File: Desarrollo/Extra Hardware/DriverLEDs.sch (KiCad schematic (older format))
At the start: 36 parts, among them J1 VCC, Q1 BC548, Q2 BC548, Q3 BC548

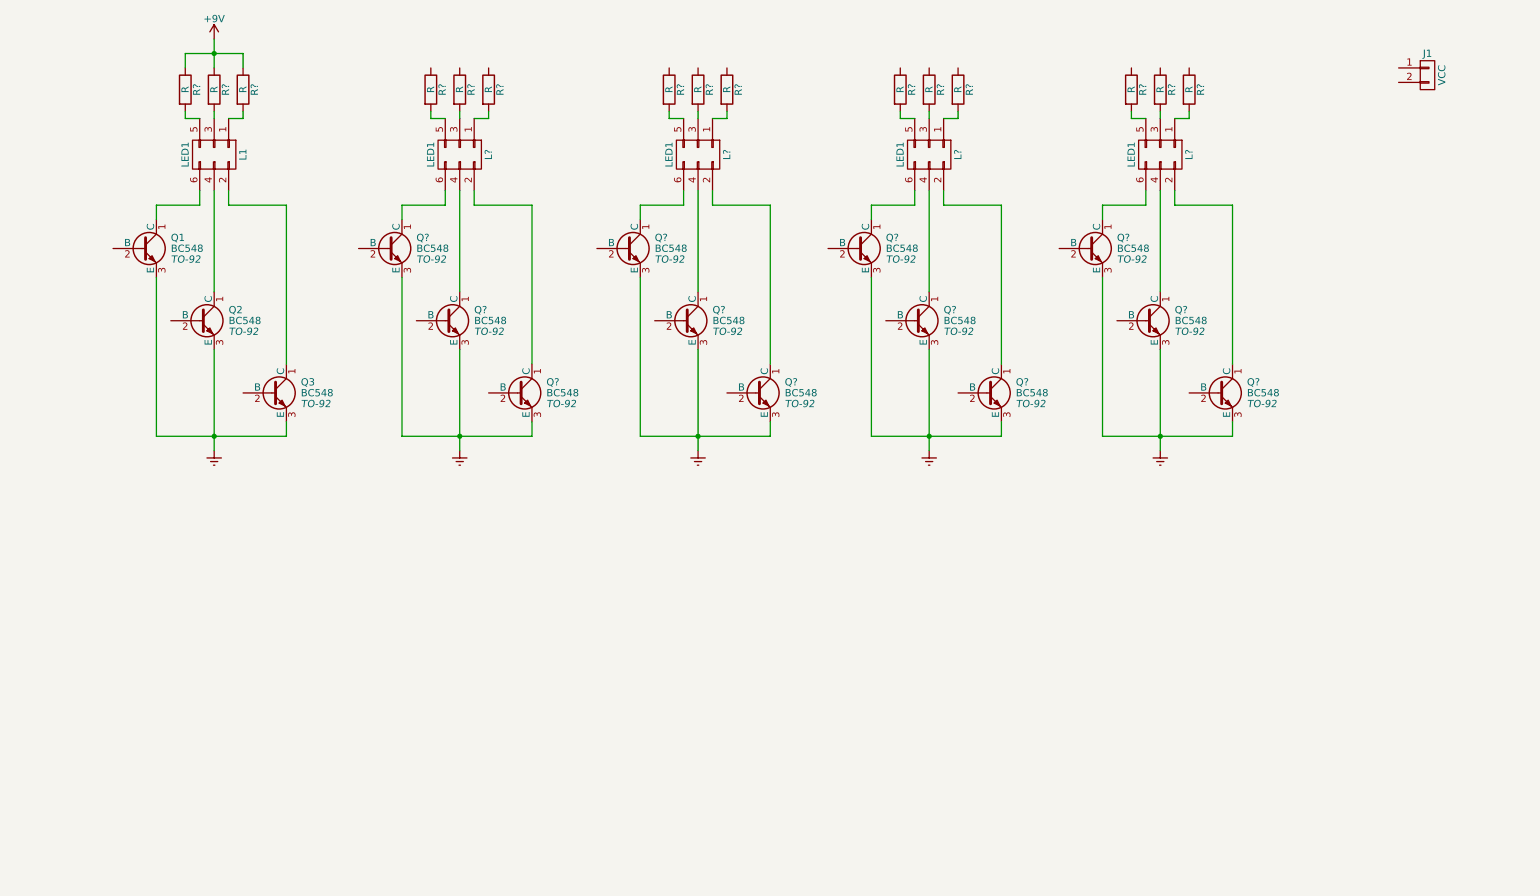
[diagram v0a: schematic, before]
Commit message: Actualización de esquemático, se completaron campos de "Hoja de dato" y "Código Digikey" para cada componente. Se completaron los rótulos de hojas. Versión Final de PCB. Actualización de tamaño de pistas y redimensión de zonas de relleno. Lista de Materiales actualizada en carpeta "Documentación".
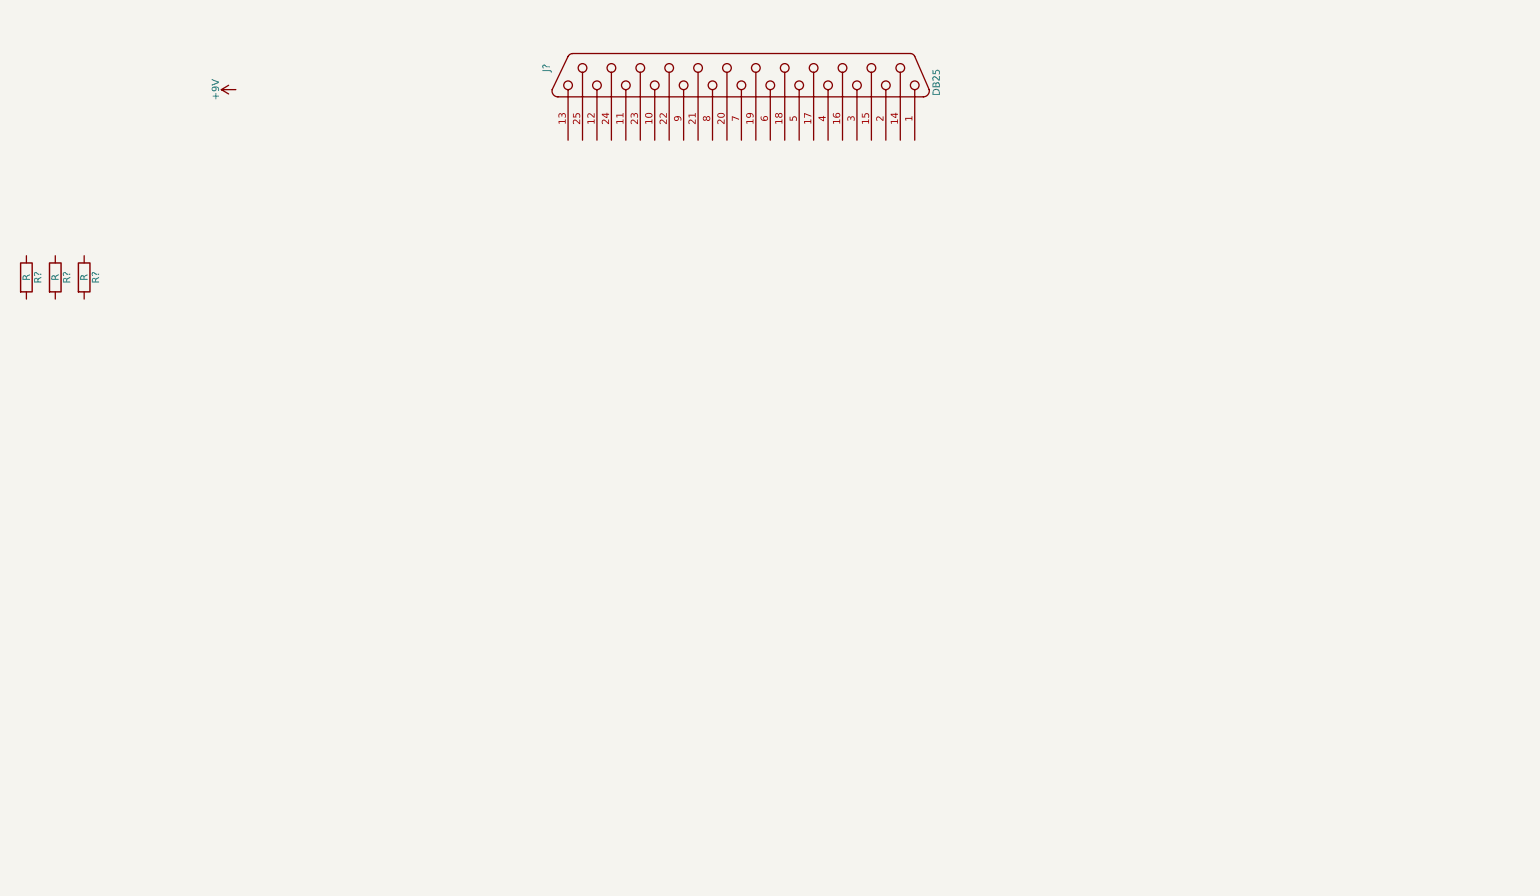
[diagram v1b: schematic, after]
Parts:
- removed J1: VCC, symbol CONN_01X02
- removed L1, L? (x4): LED1, symbol CONN_02X03
- removed Q1, Q2, Q3, Q? (x12): BC548, TO-92, symbol BC548
- removed R? (x15): R, symbol R
- added J?: DB25, symbol DB25
- added R? (x3): R, symbol R

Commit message: Desarrollo de placa de driver para manejo de leds de estimulación visual. Creación de esquemático y PCB correspondiente.
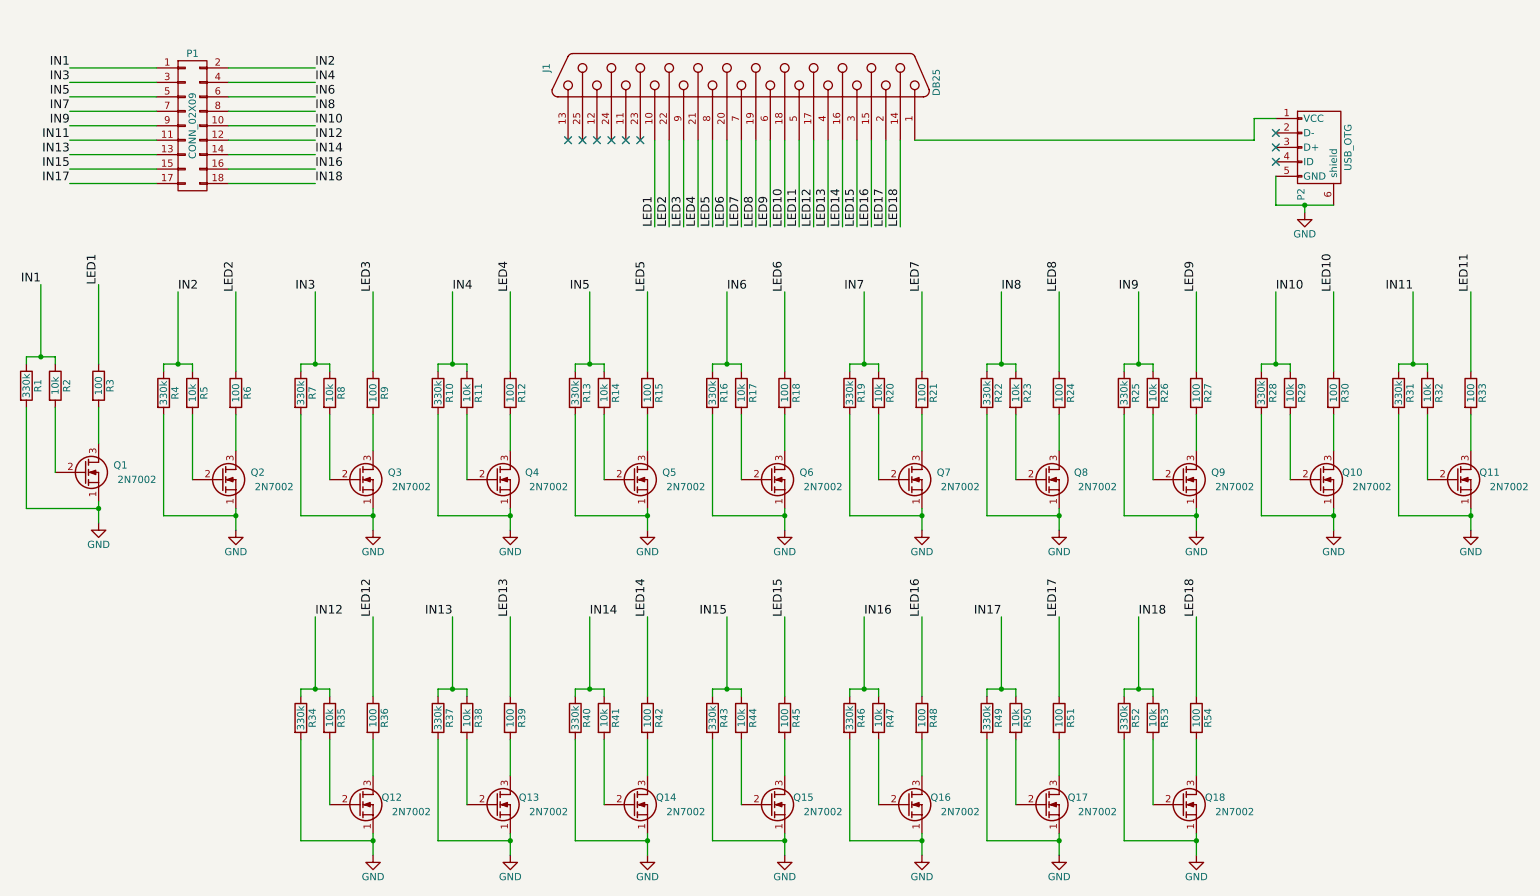
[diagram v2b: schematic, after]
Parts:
- added P1: CONN_02X09, Pin_Headers:Pin_Header_Straight_2x09, symbol CONN_02X09
- added P2: USB_OTG, Connect:USB_Micro-B, symbol USB_OTG
- added Q1, Q10, Q11, Q12, Q13, Q14, Q15, Q16, Q17, Q18, Q2, Q3, Q4, Q5, Q6, Q7, Q8, Q9: 2N7002, TO_SOT_Packages_SMD:SOT-23, symbol Q_NMOS_SGD
- added R10, R13, R16, R19, R22, R25, R28, R31, R34, R37, R4, R40, R43, R46, R49, R52, R7: 330k, DriverLeds:R_0805, symbol R
- added R11, R14, R17, R20, R23, R26, R29, R32, R35, R38, R41, R44, R47, R5, R50, R53, R8: 10k, DriverLeds:R_0805, symbol R
- added R12, R15, R18, R21, R24, R27, R30, R33, R36, R39, R42, R45, R48, R51, R54, R6, R9: 100, DriverLeds:R_0805, symbol R
- J1: renamed from J?; footprint (none) -> Connect:DB25FC
- R1: renamed from R?; value R -> 330k; footprint (none) -> DriverLeds:R_0805
- R2: renamed from R?; value R -> 10k; footprint (none) -> DriverLeds:R_0805
- R3: renamed from R?; value R -> 100; footprint (none) -> DriverLeds:R_0805
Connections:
- net at J1.1: now also P2.1 (VCC)
- net LED1: now reaches J1.10
- net LED1: now also R3.1
- net LED18: now reaches J1.14 (P14)
- net LED18: now also R54.1
- net LED16: now reaches J1.15 (P15)
- net LED16: now also R48.1
- net LED14: now reaches J1.16 (P16)
- net LED14: now also R42.1
- net LED12: now reaches J1.17 (P17)
- net LED12: now also R36.1
- net LED10: now reaches J1.18 (P18)
- net LED10: now also R30.1
- net LED8: now reaches J1.19 (P19)
- net LED8: now also R24.1
- net LED17: now reaches J1.2
- net LED17: now also R51.1
- net LED6: now reaches J1.20 (P20)
- net LED6: now also R18.1
- net LED4: now reaches J1.21 (P21)
- net LED4: now also R12.1
- net LED2: now reaches J1.22 (P22)
- net LED2: now also R6.1
- net LED15: now reaches J1.3
- net LED15: now also R45.1
- net LED13: now reaches J1.4
- net LED13: now also R39.1
- net LED11: now reaches J1.5
- net LED11: now also R33.1
- net LED9: now reaches J1.6
- net LED9: now also R27.1
- net LED7: now reaches J1.7
- net LED7: now also R21.1
- net LED5: now reaches J1.8
- net LED5: now also R15.1
- net LED3: now reaches J1.9
- net LED3: now also R9.1
- net IN1: now reaches R1.1
- net IN1: now also R2.1, P1.1 (P1)
- net GND: now reaches R1.2
- net GND: now also P2.5 (GND), P2.6 (shield), Q1.1 (S), Q10.1 (S), Q11.1 (S), Q12.1 (S), Q13.1 (S), Q14.1 (S), Q15.1 (S), Q16.1 (S), Q17.1 (S), Q18.1 (S), Q2.1 (S), Q3.1 (S), Q4.1 (S), Q5.1 (S), Q6.1 (S), Q7.1 (S), Q8.1 (S), Q9.1 (S), R10.2, R13.2, R16.2, R19.2, R22.2, R25.2, R28.2, R31.2, R34.2, R37.2, R4.2, R40.2, R43.2, R46.2, R49.2, R52.2, R7.2
- net at R2.2: now also Q1.2 (G)
- net at R3.2: now also Q1.3 (D)
- new net: Q2.2 (G), R5.2
- new net: Q2.3 (D), R6.2
- new net: Q3.2 (G), R8.2
- new net: Q3.3 (D), R9.2
- new net: Q4.2 (G), R11.2
- new net: Q4.3 (D), R12.2
- new net: Q5.2 (G), R14.2
- new net: Q5.3 (D), R15.2
- new net: Q6.2 (G), R17.2
- new net: Q6.3 (D), R18.2
- new net: Q7.2 (G), R20.2
- new net: Q7.3 (D), R21.2
- new net: Q8.2 (G), R23.2
- new net: Q8.3 (D), R24.2
- new net: Q9.2 (G), R26.2
- new net: Q9.3 (D), R27.2
- new net: Q10.2 (G), R29.2
- new net: Q10.3 (D), R30.2
- new net: Q11.2 (G), R32.2
- new net: Q11.3 (D), R33.2
- new net: Q12.2 (G), R35.2
- new net: Q12.3 (D), R36.2
- new net: Q13.2 (G), R38.2
- new net: Q13.3 (D), R39.2
- new net: Q14.2 (G), R41.2
- new net: Q14.3 (D), R42.2
- new net: Q15.2 (G), R44.2
- new net: Q15.3 (D), R45.2
- new net: Q16.2 (G), R47.2
- new net: Q16.3 (D), R48.2
- new net: Q17.2 (G), R50.2
- new net: Q17.3 (D), R51.2
- new net: Q18.2 (G), R53.2
- new net: Q18.3 (D), R54.2
- new net IN10: P1.10 (P10), R28.1, R29.1
- new net IN11: P1.11 (P11), R31.1, R32.1
- new net IN12: P1.12 (P12), R34.1, R35.1
- new net IN13: P1.13 (P13), R37.1, R38.1
- new net IN14: P1.14 (P14), R40.1, R41.1
- new net IN15: P1.15 (P15), R43.1, R44.1
- new net IN16: P1.16 (P16), R46.1, R47.1
- new net IN17: P1.17 (P17), R49.1, R50.1
- new net IN18: P1.18 (P18), R52.1, R53.1
- new net IN2: P1.2 (P2), R4.1, R5.1
- new net IN3: P1.3 (P3), R7.1, R8.1
- new net IN4: P1.4 (P4), R10.1, R11.1
- new net IN5: P1.5 (P5), R13.1, R14.1
- new net IN6: P1.6 (P6), R16.1, R17.1
- new net IN7: P1.7 (P7), R19.1, R20.1
- new net IN8: P1.8 (P8), R22.1, R23.1
- new net IN9: P1.9 (P9), R25.1, R26.1
- no-connect marks 0 -> 9
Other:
- moved on the sheet: R1, R2, R3
